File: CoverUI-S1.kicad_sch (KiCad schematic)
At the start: 37 parts, among them J2 Conn_01x36_MountingPin, J5 Conn_01x06_Pin, J6 Conn_01x04_Pin, J7 Conn_01x03_Pin, U1 Top-Stop-Hall, U2 74AHC1G32

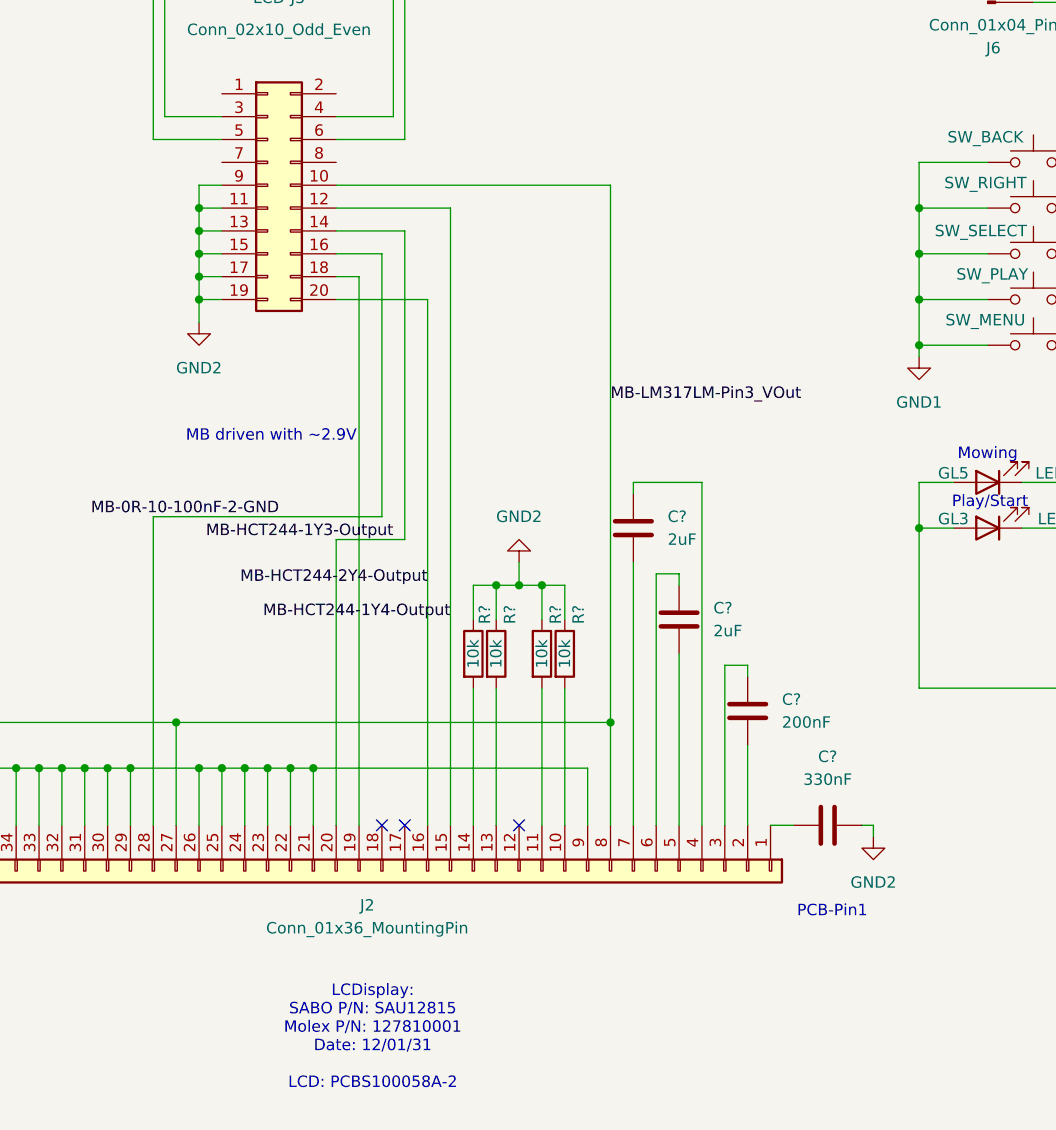
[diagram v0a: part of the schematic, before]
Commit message: Recent v0.1 and CoverUI discoveries
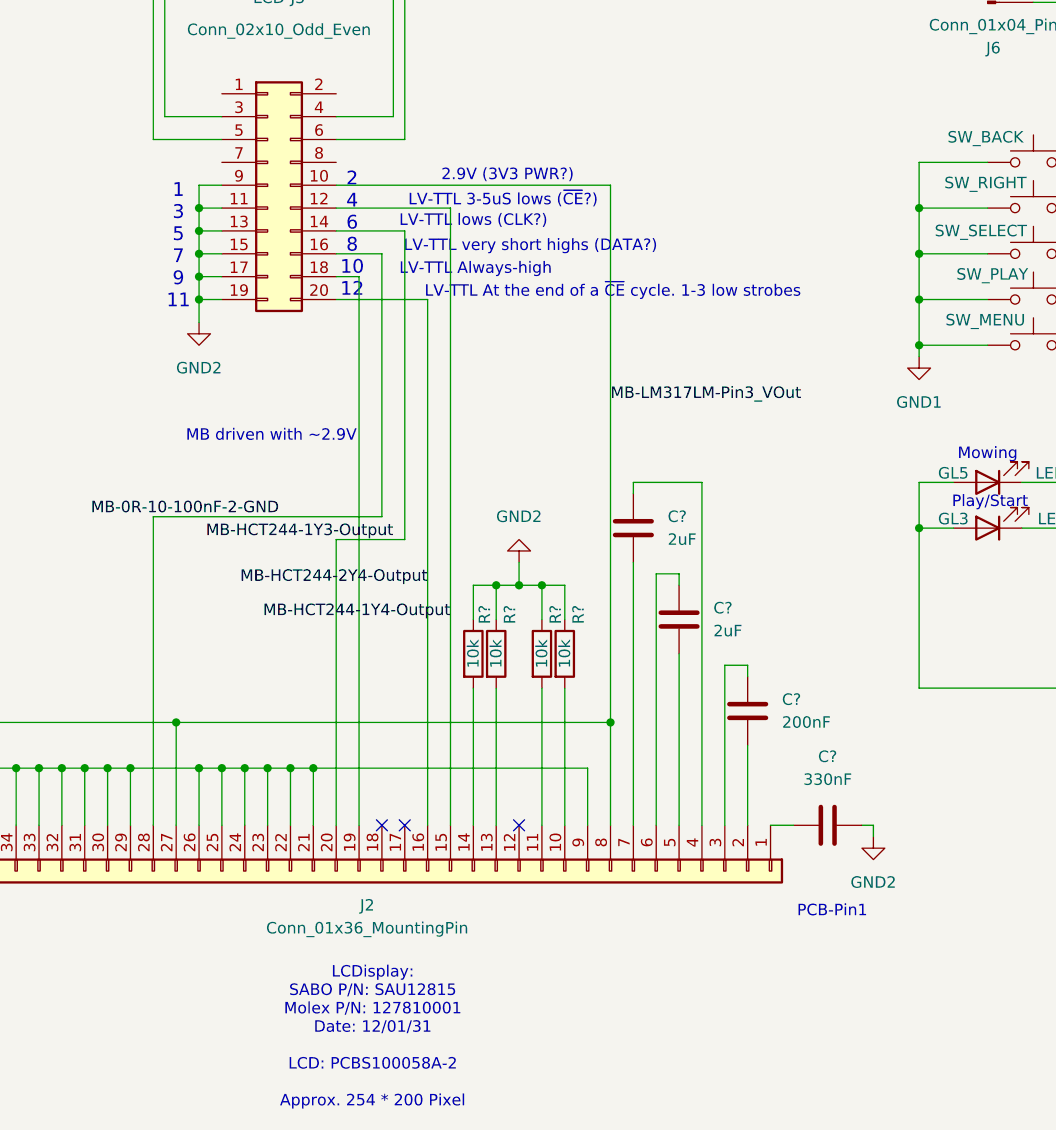
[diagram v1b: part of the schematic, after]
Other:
- note added: "1 3 5 7 9 11"
- note added: "2 4 6 8 10 12"
- note added: "2.9V (3V3 PWR?)"
- note added: "LCDisplay: SABO P/N: SAU12815 Molex P/N: 127810001 Date: 12/01/31 LCD: PCBS100058A-2 Approx. 254 * 200 Pixel"
- note added: "LV-TTL 3-5uS lows (~{CE}?)"
- note added: "LV-TTL Always-high"
- note added: "LV-TTL At the end of a ~{CE} cycle. 1-3 low strobes"
- note added: "LV-TTL lows (CLK?)"
- note added: "LV-TTL very short highs (DATA?)"
- note removed: "LCDisplay: SABO P/N: SAU12815 Molex P/N: 127810001 Date: 12/01/31 LCD: PCBS100058A-2"
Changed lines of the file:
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@@
 		(rev "v0.1")
+	)
+	(text "LV-TTL Always-high"
+		(exclude_from_sim no)
+		(at 90.424 86.868 0)
+		(effects
+			(font
+				(size 1.27 1.27)
+			)
+		)
 	)
 	(text "?"
@@
 		(exclude_from_sim no)
 		(at 147.574 112.776 0)
+		(effects
+			(font
+				(size 1.27 1.27)
+			)
+		)
+	)
+	(text "LV-TTL lows (CLK?)"
+		(exclude_from_sim no)
+		(at 90.17 81.534 0)
+		(effects
+			(font
+				(size 1.27 1.27)
+			)
+		)
+	)
+	(text "LV-TTL 3-5uS lows (~{CE}?)"
+		(exclude_from_sim no)
+		(at 93.472 79.248 0)
 		(effects
 			(font
@@
 		)
 	)
+	(text "LV-TTL At the end of a ~{CE} cycle. 1-3 low strobes"
+		(exclude_from_sim no)
+		(at 105.664 89.408 0)
+		(effects
+			(font
+				(size 1.27 1.27)
+			)
+		)
+	)
+	(text "1\n3\n5\n7\n9\n11"
+		(exclude_from_sim no)
+		(at 57.404 84.328 0)
+		(effects
+			(font
+				(size 1.524 1.524)
+			)
+		)
+	)
 	(text "Plug-Pin1"
 		(exclude_from_sim no)
@@
 		)
 	)
-	(text "LCDisplay:\nSABO P/N: SAU12815\nMolex P/N: 127810001\nDate: 12/01/31\n\nLCD: PCBS100058A-2"
+	(text "2.9V (3V3 PWR?)"
+		(exclude_from_sim no)
+		(at 93.98 76.454 0)
+		(effects
+			(font
+				(size 1.27 1.27)
+			)
+		)
+	)
+	(text "LV-TTL very short highs (DATA?)"
+		(exclude_from_sim no)
+		(at 96.52 84.328 0)
+		(effects
+			(font
+				(size 1.27 1.27)
+			)
+		)
+	)
+	(text "2\n4\n6\n8\n10\n12"
+		(exclude_from_sim no)
+		(at 76.708 83.058 0)
+		(effects
+			(font
+				(size 1.524 1.524)
+			)
+		)
+	)
+	(text "LCDisplay:\nSABO P/N: SAU12815\nMolex P/N: 127810001\nDate: 12/01/31\n\nLCD: PCBS100058A-2\n\nApprox. 254 * 200 Pixel"
 		(exclude_from_sim no)
 		(at 78.994 172.212 0)

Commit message: Finish v0.2 schematic and ERC
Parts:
- C?: value 330nF -> ~330nF
- C?: value 200nF -> ~200nF
- C? (x2): value 2uF -> ~2uF
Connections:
- net -> OEM HC126 P6 (2Y): now reaches J2.19 (Pin_19), LCD-J3.18 (Pin_18)
- net MB-0R-10-100nF-2-GND renamed -> OEM HC126 P3 (1Y)
- net MB-HCT244-1Y3-Output renamed -> OEM HC126 P11 (4Y)
- net MB-HCT244-1Y4-Output renamed -> OEM HC126 P8 (3Y)
- net MB-HCT244-2Y4-Output renamed -> OEM SOIC?-5 LDO? "W33" P4 (EN?)
- net MB-LM317LM-Pin3_VOut renamed -> OEM LM317 2.9V Out
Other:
- note added: "1 3 Debug- 5 Cable 7 9 11"
- note removed: "1 3 5 7 9 11"
- note removed: "2.9V (3V3 PWR?)"
- note removed: "LV-TTL 3-5uS lows (~{CE}?)"
- note removed: "LV-TTL Always-high"
- note removed: "LV-TTL At the end of a ~{CE} cycle. 1-3 low strobes"
- note removed: "LV-TTL lows (CLK?)"
- note removed: "LV-TTL very short highs (DATA?)"
- note removed: "MB driven with ~2.9V"
- moved on the sheet: D1, LCD-J3
